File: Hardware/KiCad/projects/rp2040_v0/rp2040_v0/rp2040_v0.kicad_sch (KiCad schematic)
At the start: 52 parts, among them J1 Conn_01x03, J10 Conn_01x01, J11 Conn_01x02, J12 Screw_Terminal_01x02, J2 Conn_01x02, J3 Conn_01x03, J4 Conn_01x01, J5 USB_B_Micro, J6 Conn_01x01, J7 Conn_01x01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

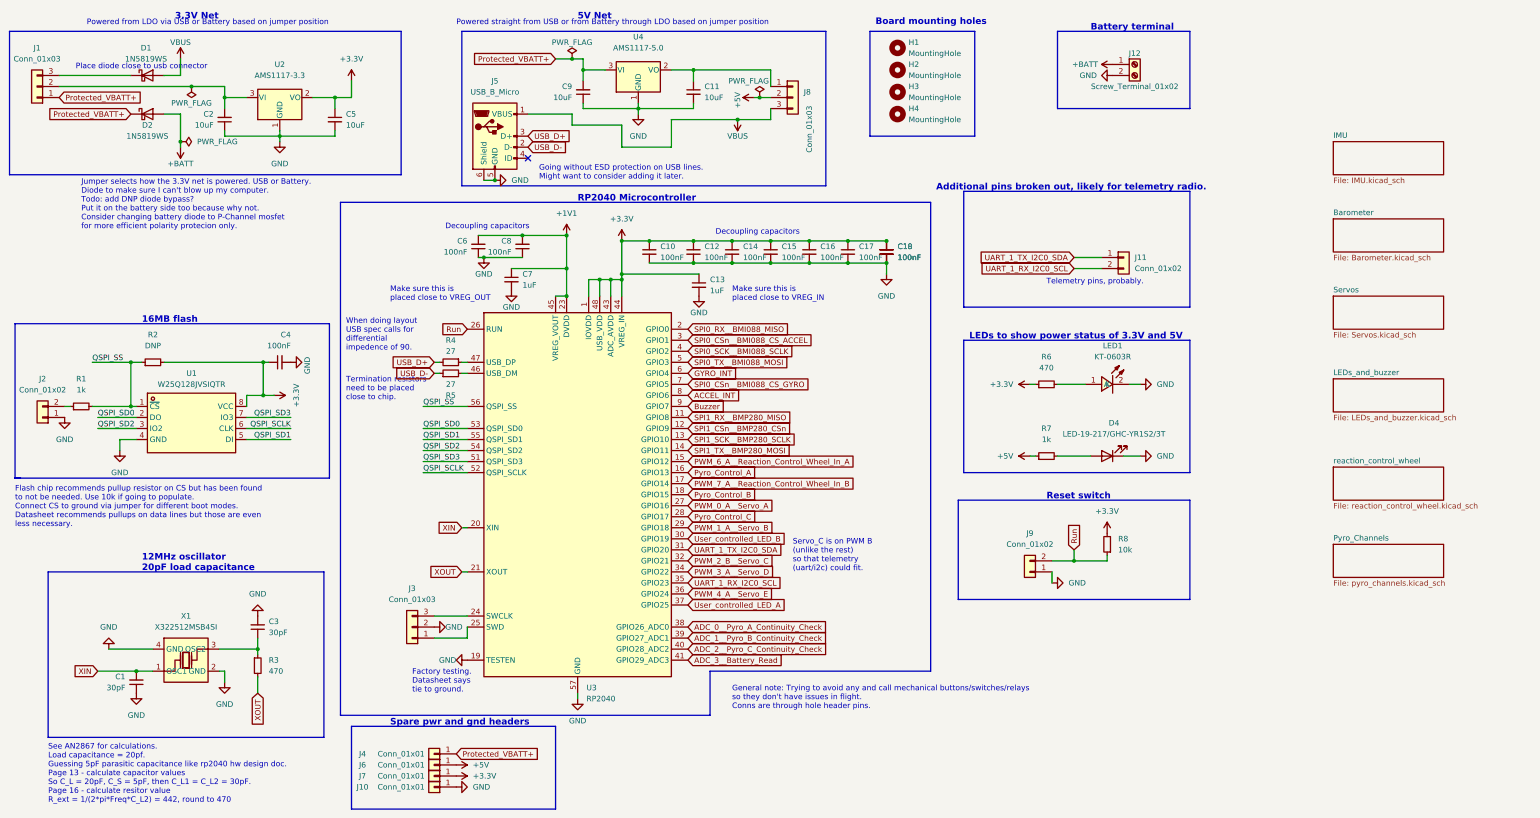
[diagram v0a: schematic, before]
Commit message: CRITICAL MISTAKE FOUND. FIXED. Flash was wired wrong. Add versioning sheet.
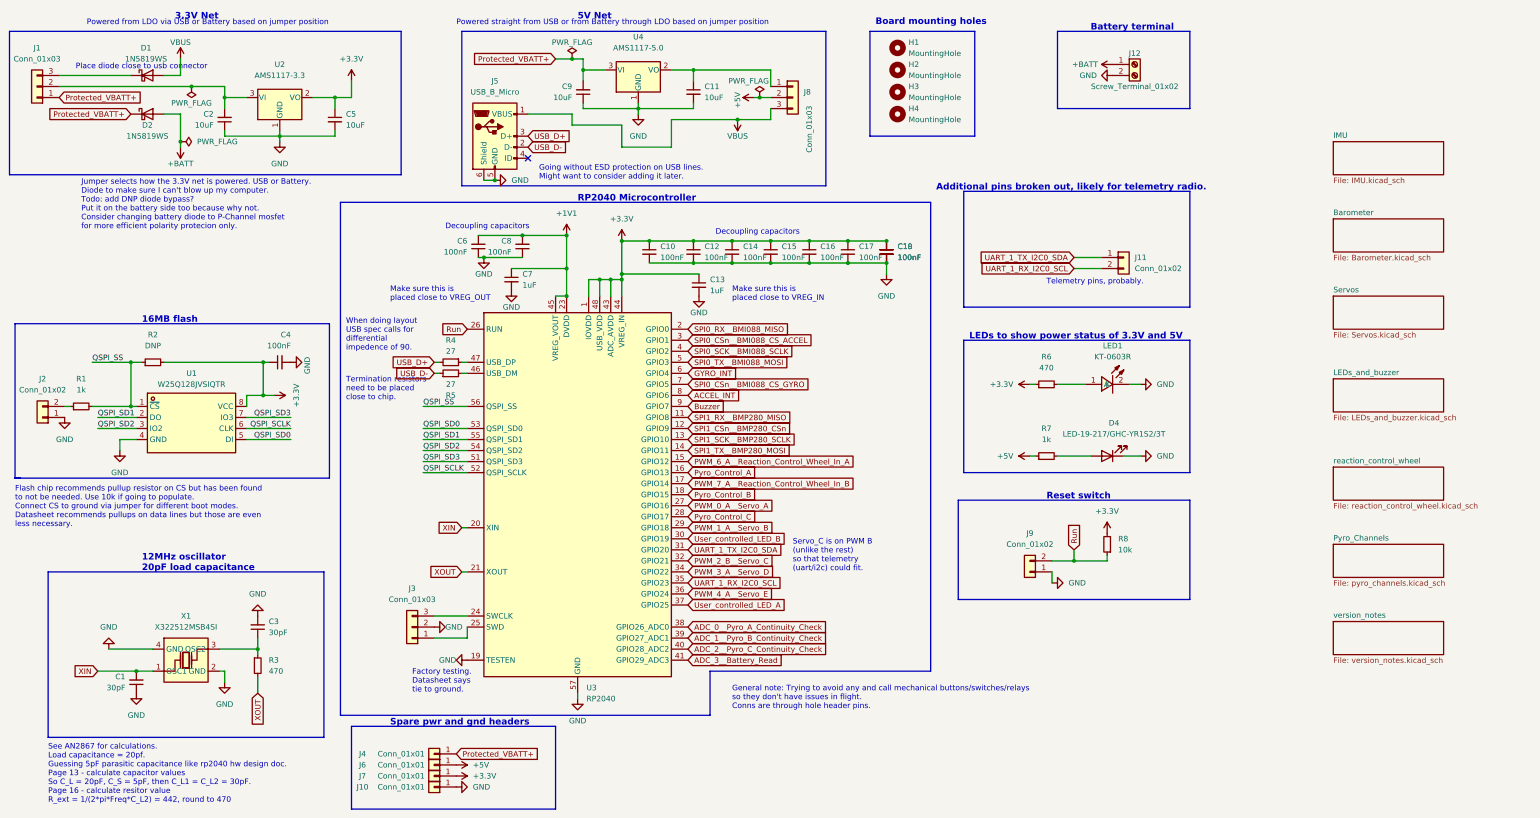
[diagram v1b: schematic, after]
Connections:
- net QSPI_SD0: now also U1.5 (DI); no longer U1.2 (DO)
- net QSPI_SD1: now also U1.2 (DO); no longer U1.5 (DI)
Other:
- added sheet version_notes (version_notes.kicad_sch)
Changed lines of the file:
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@@
   (title_block
     (title "rp2040 Flight Computer")
-    (date "2023-01-29")
-    (rev "v0.1")
+    (date "2023-01-30")
+    (rev "v0.2")
   )
   (junction (at 185.42 33.02) (diameter 0) (color 0 0 0 0)
@@
     (effects (font (size 1.27 1.27)) (justify left bottom))
   )
-  (label "QSPI_SD1" (at 77.47 111.76 180)
+  (label "QSPI_SD0" (at 77.47 111.76 180)
     (effects (font (size 1.27 1.27)) (justify right bottom))
   )
@@
     (effects (font (size 1.27 1.27)) (justify right bottom))
   )
-  (label "QSPI_SD0" (at 33.02 106.68 0)
+  (label "QSPI_SD1" (at 33.02 106.68 0)
     (effects (font (size 1.27 1.27)) (justify left bottom))
   )
@@
     (pin "2")
   )
+  (sheet (at 317.5 153.67) (size 25.4 7.62) (fields_autoplaced)
+    (stroke (width 0.1524) (type solid) (color 0 0 0 0))
+    (fill (color 0 0 0 0.0000))
+    (property "Sheet name" "version_notes" (id 0) (at 317.5 152.9584 0)
+      (effects (font (size 1.27 1.27)) (justify left bottom))
+    )
+    (property "Sheet file" "version_notes.kicad_sch" (id 1) (at 317.5 161.8746 0)
+      (effects (font (size 1.27 1.27)) (justify left top))
+    )
+  )
   (sheet (at 317.5 135.89) (size 25.4 7.62) (fields_autoplaced)
     (stroke (width 0.1524) (type solid) (color 0 0 0 0))
@@
     (path "/848a71b8-bab3-424a-a51e-99629cb440e3" (page "6"))
     (path "/5973b2d7-3984-4261-9bd9-41fa219882e0" (page "7"))
+    (path "/098ef3f0-85bb-45b0-9fcd-f86fb9cd9978" (page "8"))
   )
   (symbol_instances

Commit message: Change LEDs to be kicad versions using kicad footprints for consistancy.
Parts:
- removed LED1: KT-0603R, easyeda2kicad:LED0603-R-RD, symbol easyeda2kicad_flight_computer:KT-0603R
- added D6: LED-KT-0603R, LED_SMD:LED_0603_1608Metric, symbol Device:LED
- D4: footprint easyeda2kicad:LED0603-R-RD -> LED_SMD:LED_0603_1608Metric
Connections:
- net GND: now also D6.1 (K)
- net at R6.2: now also D6.2 (A)
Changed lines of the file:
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@@
     (stroke (width 0) (type default) (color 0 0 0 0))
   )
-  (wire (pts (xy 254 99.06) (xy 260.35 99.06))
+  (wire (pts (xy 254 99.06) (xy 261.62 99.06))
     (stroke (width 0) (type default) (color 0 0 0 0))
   )
@@
     (stroke (width 0) (type default) (color 0 0 0 0))
   )
-  (wire (pts (xy 270.51 99.06) (xy 273.05 99.06))
+  (wire (pts (xy 269.24 99.06) (xy 273.05 99.06))
     (stroke (width 0) (type default) (color 0 0 0 0))
   )
@@
     (pin "2")
   )
+  (symbol (lib_id "Device:LED") (at 265.43 99.06 180) (unit 1)
+    (in_bom yes) (on_board yes) (fields_autoplaced)
+    (property "Reference" "D6" (id 0) (at 267.0175 91.44 0))
+    (property "Value" "LED-KT-0603R" (id 1) (at 267.0175 93.98 0))
+    (property "Footprint" "LED_SMD:LED_0603_1608Metric" (id 2) (at 265.43 99.06 0)
+      (effects (font (size 1.27 1.27)) hide)
+    )
+    (property "Datasheet" "~" (id 3) (at 265.43 99.06 0)
+      (effects (font (size 1.27 1.27)) hide)
+    )
+    (pin "1")
+    (pin "2")
+  )
   (symbol (lib_id "Connector:Screw_Terminal_01x02") (at 271.78 25.4 0) (unit 1)
     (in_bom yes) (on_board yes)
@@
     (property "Reference" "D4" (id 0) (at 267.0175 107.95 0))
     (property "Value" "LED-19-217/GHC-YR1S2/3T" (id 1) (at 267.0175 110.49 0))
-    (property "Footprint" "easyeda2kicad:LED0603-R-RD" (id 2) (at 265.43 115.57 0)
+    (property "Footprint" "LED_SMD:LED_0603_1608Metric" (id 2) (at 265.43 115.57 0)
       (effects (font (size 1.27 1.27)) hide)
     )
@@
     (pin "2")
   )
-  (symbol (lib_id "easyeda2kicad_flight_computer:KT-0603R") (at 265.43 97.79 180) (unit 1)
-    (in_bom yes) (on_board yes) (fields_autoplaced)
-    (property "Reference" "LED1" (id 0) (at 266.7 90.17 0))
-    (property "Value" "KT-0603R" (id 1) (at 266.7 92.71 0))
-    (property "Footprint" "easyeda2kicad:LED0603-R-RD" (id 2) (at 265.43 91.44 0)
-      (effects (font (size 1.27 1.27)) hide)
-    )
-    (property "Datasheet" "https://lcsc.com/product-detail/Light-Emitting-Diodes-LED_Red-LED-0603_C2286.html" (id 3) (at 265.43 88.9 0)
-      (effects (font (size 1.27 1.27)) hide)
-    )
-    (property "LCSC Part" "C2286" (id 4) (at 265.43 86.36 0)
-      (effects (font (size 1.27 1.27)) hide)
-    )
-    (property "JLC Part" "Basic Part" (id 5) (at 265.43 83.82 0)
-      (effects (font (size 1.27 1.27)) hide)
-    )
-    (pin "1")
-    (pin "2")
-  )
   (symbol (lib_id "power:GND") (at 124.46 52.07 90) (unit 1)
     (in_bom yes) (on_board yes) (fields_autoplaced)
@@
     )
     (path "/80e37a29-2645-40c2-ad1a-3b8bdd51b77d/665cb1a8-2553-4509-888c-4a9467621ea3"
-      (reference "D3") (unit 1) (value "LED-19-217/GHC-YR1S2/3T") (footprint "easyeda2kicad:LED0603-R-RD")
+      (reference "D3") (unit 1) (value "LED-19-217/GHC-YR1S2/3T") (footprint "LED_SMD:LED_0603_1608Metric")
     )
     (path "/8df9ca35-88fa-4949-b71c-f8ff3b451cf1"
-      (reference "D4") (unit 1) (value "LED-19-217/GHC-YR1S2/3T") (footprint "easyeda2kicad:LED0603-R-RD")
+      (reference "D4") (unit 1) (value "LED-19-217/GHC-YR1S2/3T") (footprint "LED_SMD:LED_0603_1608Metric")
+    )
+    (path "/80e37a29-2645-40c2-ad1a-3b8bdd51b77d/7b4e9da8-1f2a-4881-918c-03b67057b0a6"
+      (reference "D5") (unit 1) (value "LED-KT-0603R") (footprint "LED_SMD:LED_0603_1608Metric")
+    )
+    (path "/3ecbfa75-727e-44ce-99bc-aec6f252e8db"
+      (reference "D6") (unit 1) (value "LED-KT-0603R") (footprint "LED_SMD:LED_0603_1608Metric")
     )
     (path "/64d28788-7fbc-4281-8f3a-ddcbca4cafbb"
@@
       (reference "J12") (unit 1) (value "Screw_Terminal_01x02") (footprint "easyeda2kicad:CONN-TH_XY301V-A-5.0-2P")
     )
-    (path "/e2b4e37d-6e5e-4589-9577-9e6c278210bd/d2a54fd5-7919-4c91-b875-5b1a6fb2c212"
-      (reference "J13") (unit 1) (value "Conn_02x09_Counter_Clockwise") (footprint "Connector_PinHeader_2.54mm:PinHeader_2x09_P2.54mm_Vertical")
+    (path "/e2b4e37d-6e5e-4589-9577-9e6c278210bd/9c130a7d-a3a5-46d1-a551-4509fd300e50"
+      (reference "J13") (unit 1) (value "Conn_02x09_Odd_Even") (footprint "Connector_PinHeader_2.54mm:PinHeader_2x09_P2.54mm_Vertical")
     )
     (path "/af425a44-c1bd-47e9-b36b-bb47c607ce87/761ab2ce-df5f-409b-967d-1e959fa3465f"
@@
       (reference "J28") (unit 1) (value "Screw_Terminal_01x02") (footprint "easyeda2kicad:CONN-TH_XY301V-A-5.0-2P")
     )
-    (path "/e648d3b1-eed1-4f79-8d45-25203286cbe0"
-      (reference "LED1") (unit 1) (value "KT-0603R") (footprint "easyeda2kicad:LED0603-R-RD")
-    )
-    (path "/80e37a29-2645-40c2-ad1a-3b8bdd51b77d/bb235dc0-0e75-4366-9159-753685d94dd0"
-      (reference "LED2") (unit 1) (value "KT-0603R") (footprint "easyeda2kicad:LED0603-R-RD")
-    )
     (path "/80e37a29-2645-40c2-ad1a-3b8bdd51b77d/3352021c-8cb8-42ec-98cf-2673b66b0156"

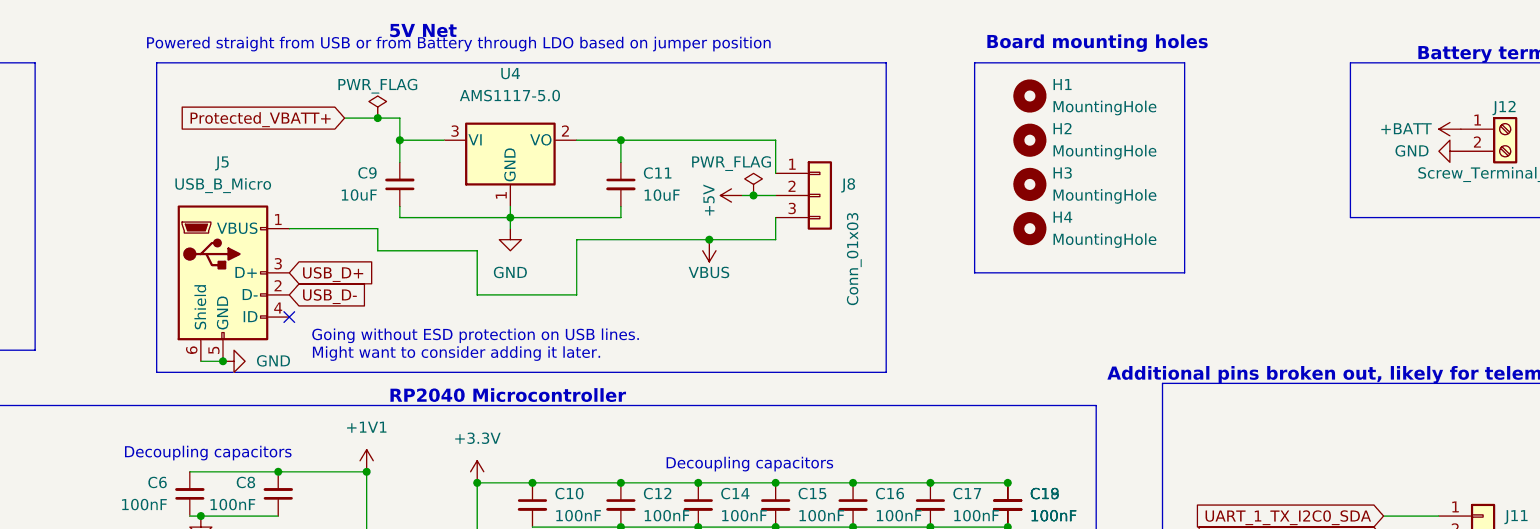
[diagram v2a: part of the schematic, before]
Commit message: Add note on raw usb power to schematic
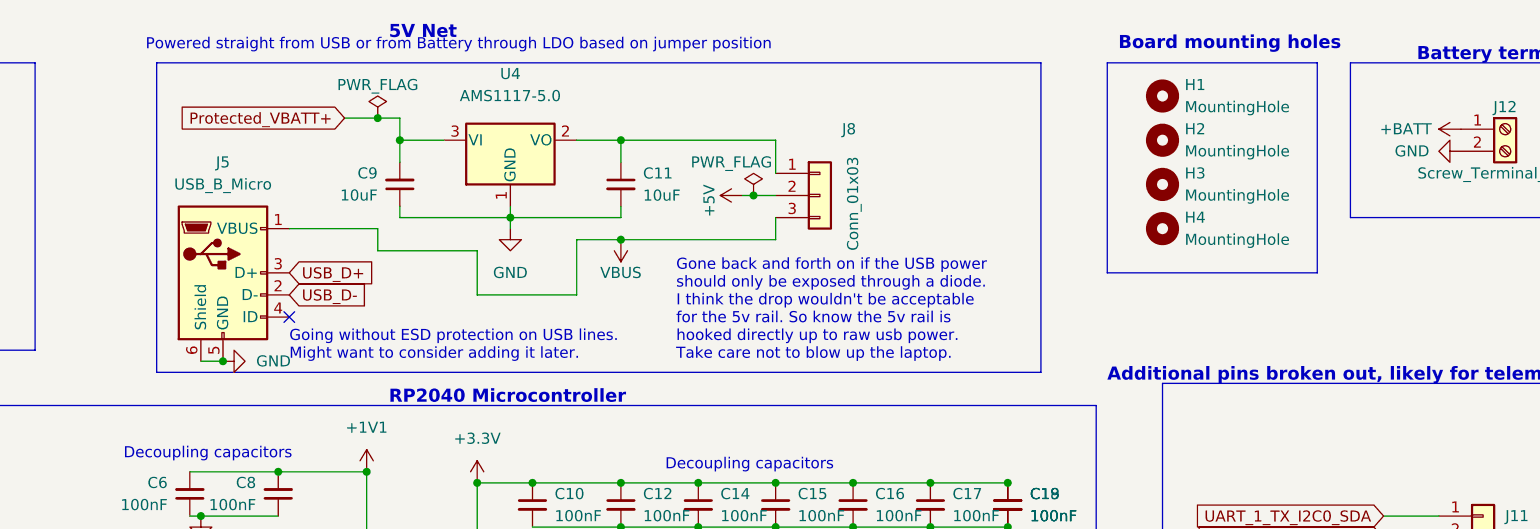
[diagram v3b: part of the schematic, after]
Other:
- note added: "Gone back and forth on if the USB power should only be exposed through a diode. I think the drop wouldn't be acceptable for the 5v rail. So know the 5v rail is hooked directly up to raw usb power. Take care not to blow up the laptop."
- moved on the sheet: H1, H2, H3, H4

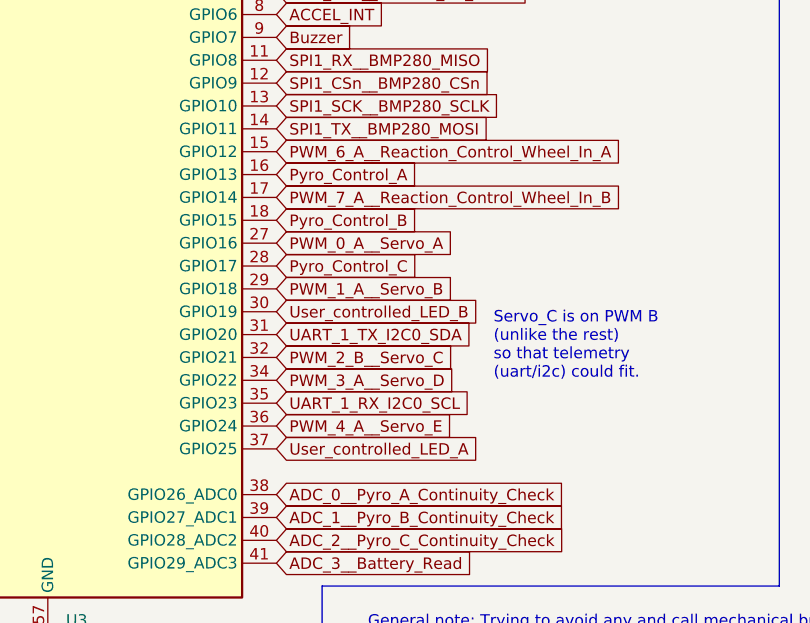
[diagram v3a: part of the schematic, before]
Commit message: witch led and pyro pins for easier routing
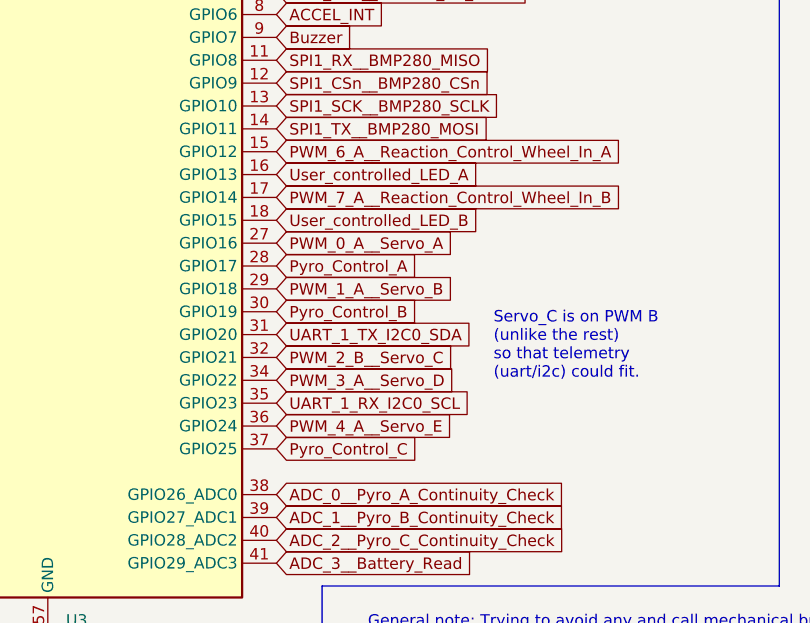
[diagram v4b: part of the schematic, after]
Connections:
- net Pyro_Control_A: now also U3.28 (GPIO17); no longer U3.16 (GPIO13)
- net Pyro_Control_B: now also U3.30 (GPIO19); no longer U3.18 (GPIO15)
- net Pyro_Control_C: now also U3.37 (GPIO25); no longer U3.28 (GPIO17)
- net User_controlled_LED_A: now also U3.16 (GPIO13); no longer U3.37 (GPIO25)
- net User_controlled_LED_B: now also U3.18 (GPIO15); no longer U3.30 (GPIO19)
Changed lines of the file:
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@@
     )
   )
-  (global_label "Pyro_Control_A" (shape input) (at 168.91 119.38 0) (fields_autoplaced)
-    (effects (font (size 1.27 1.27)) (justify left))
-    (property "Intersheet References" "${INTERSHEET_REFS}" (id 0) (at 177.6731 119.3006 0)
+  (global_label "Pyro_Control_A" (shape input) (at 168.91 129.54 0) (fields_autoplaced)
+    (effects (font (size 1.27 1.27)) (justify left))
+    (property "Intersheet References" "${INTERSHEET_REFS}" (id 0) (at 177.6731 129.4606 0)
       (effects (font (size 1.27 1.27)) (justify left) hide)
     )
@@
     )
   )
-  (global_label "User_controlled_LED_A" (shape input) (at 168.91 149.86 0) (fields_autoplaced)
-    (effects (font (size 1.27 1.27)) (justify left))
-    (property "Intersheet References" "${INTERSHEET_REFS}" (id 0) (at 192.6107 149.7806 0)
+  (global_label "User_controlled_LED_A" (shape input) (at 168.91 119.38 0) (fields_autoplaced)
+    (effects (font (size 1.27 1.27)) (justify left))
+    (property "Intersheet References" "${INTERSHEET_REFS}" (id 0) (at 192.6107 119.3006 0)
       (effects (font (size 1.27 1.27)) (justify left) hide)
     )
@@
     )
   )
-  (global_label "Pyro_Control_C" (shape input) (at 168.91 129.54 0) (fields_autoplaced)
-    (effects (font (size 1.27 1.27)) (justify left))
-    (property "Intersheet References" "${INTERSHEET_REFS}" (id 0) (at 177.6731 129.4606 0)
+  (global_label "Pyro_Control_C" (shape input) (at 168.91 149.86 0) (fields_autoplaced)
+    (effects (font (size 1.27 1.27)) (justify left))
+    (property "Intersheet References" "${INTERSHEET_REFS}" (id 0) (at 177.6731 149.7806 0)
       (effects (font (size 1.27 1.27)) (justify left) hide)
     )
@@
     )
   )
-  (global_label "Pyro_Control_B" (shape input) (at 168.91 124.46 0) (fields_autoplaced)
-    (effects (font (size 1.27 1.27)) (justify left))
-    (property "Intersheet References" "${INTERSHEET_REFS}" (id 0) (at 177.6731 124.3806 0)
+  (global_label "Pyro_Control_B" (shape input) (at 168.91 134.62 0) (fields_autoplaced)
+    (effects (font (size 1.27 1.27)) (justify left))
+    (property "Intersheet References" "${INTERSHEET_REFS}" (id 0) (at 177.6731 134.5406 0)
       (effects (font (size 1.27 1.27)) (justify left) hide)
     )
@@
     )
   )
-  (global_label "User_controlled_LED_B" (shape input) (at 168.91 134.62 0) (fields_autoplaced)
-    (effects (font (size 1.27 1.27)) (justify left))
-    (property "Intersheet References" "${INTERSHEET_REFS}" (id 0) (at 192.7921 134.6994 0)
-      (effects (font (size 1.27 1.27)) (justify left) hide)
-    )
+  (global_label "User_controlled_LED_B" (shape input) (at 168.91 124.46 0) (fields_autoplaced)
+    (effects (font (size 1.27 1.27)) (justify left))
+    (property "Intersheet References" "${INTERSHEET_REFS}" (id 0) (at 192.7921 124.5394 0)
+      (effects (font (size 1.27 1.27)) (justify left) hide)
+    )
